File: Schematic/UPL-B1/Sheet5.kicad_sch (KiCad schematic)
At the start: 103 parts, among them P53 TestPoint, P54 TestPoint, P55 TestPoint, P56 TestPoint, P57 TestPoint, P58 TestPoint, X50 Conn_01x03_Pin_Bridge, X51 Conn_01x03_Pin_Bridge, X52 Conn_01x03_Pin_Bridge

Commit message: Add device datasheets, begin migration to hierarchical labels
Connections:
- net LDFREQ renamed LOFREQ
- no-connect marks 0 -> 2
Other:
- note added: "+/- ~15V"
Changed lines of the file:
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@@
 		)
 	)
+	(text "+/- ~15V"
+		(exclude_from_sim no)
+		(at 81.026 191.516 0)
+		(effects
+			(font
+				(size 1.27 1.27)
+			)
+		)
+	)
 	(text "SHEET 6"
 		(exclude_from_sim no)
@@
 		(color 0 0 0 0)
 	)
+	(no_connect
+		(at 353.06 171.45)
+	)
+	(no_connect
+		(at 383.54 171.45)
+	)
 	(wire
 		(pts
@@
 	(global_label "SIN"
 		(shape input)
-		(at 43.18 270.51 180)
+		(at 374.65 226.06 180)
 		(fields_autoplaced yes)
 		(effects
@@
 		)
 		(property "Intersheetrefs" "${INTERSHEET_REFS}"
-			(at 37.05 270.51 0)
+			(at 368.52 226.06 0)
 			(effects
 				(font
@@
 		)
 	)
-	(global_label "SIN"
+	(hierarchical_label "SIN"
 		(shape input)
-		(at 374.65 226.06 180)
-		(fields_autoplaced yes)
+		(at 43.18 270.51 180)
 		(effects
 			(font
@@
 			(justify right)
 		)
-		(property "Intersheetrefs" "${INTERSHEET_REFS}"
-			(at 368.52 226.06 0)
-			(effects
-				(font
-					(size 1.27 1.27)
-				)
-				(justify right)
-				(hide yes)
-			)
-		)
 	)
-	(global_label "FILT"
+	(hierarchical_label "FILT"
 		(shape input)
 		(at 43.18 191.77 180)
-		(fields_autoplaced yes)
 		(effects
 			(font
@@
 			(justify right)
 		)
-		(property "Intersheetrefs" "${INTERSHEET_REFS}"
-			(at 36.5057 191.77 0)
-			(effects
-				(font
-					(size 1.27 1.27)
-				)
-				(justify right)
-				(hide yes)
-			)
-		)
-	)
-	(global_label "FREQ_ENA"
-		(shape output)
-		(at 317.5 270.51 0)
-		(fields_autoplaced yes)
-		(effects
-			(font
-				(size 1.27 1.27)
-			)
-			(justify left)
-		)
-		(property "Intersheetrefs" "${INTERSHEET_REFS}"
-			(at 329.859 270.51 0)
-			(effects
-				(font
-					(size 1.27 1.27)
-				)
-				(justify left)
-				(hide yes)
-			)
-		)
 	)
-	(global_label "LDFREQ"
+	(hierarchical_label "LOFREQ"
 		(shape output)
 		(at 317.5 283.21 0)
-		(fields_autoplaced yes)
 		(effects
 			(font
@@
 			(justify left)
 		)
-		(property "Intersheetrefs" "${INTERSHEET_REFS}"
-			(at 327.6214 283.21 0)
-			(effects
-				(font
-					(size 1.27 1.27)
-				)
-				(justify left)
-				(hide yes)
-			)
-		)
 	)
-	(global_label "COS"
+	(hierarchical_label "COS"
 		(shape input)
 		(at 41.91 162.56 180)
-		(fields_autoplaced yes)
 		(effects
 			(font
@@
 			(justify right)
 		)
-		(property "Intersheetrefs" "${INTERSHEET_REFS}"
-			(at 35.1148 162.56 0)
-			(effects
-				(font
-					(size 1.27 1.27)
-				)
-				(justify right)
-				(hide yes)
-			)
-		)
 	)
-	(global_label "ALC"
+	(hierarchical_label "ALC"
 		(shape output)
 		(at 563.88 229.87 0)
-		(fields_autoplaced yes)
 		(effects
 			(font
@@
 			(justify left)
 		)
-		(property "Intersheetrefs" "${INTERSHEET_REFS}"
-			(at 570.2519 229.87 0)
-			(effects
-				(font
-					(size 1.27 1.27)
-				)
-				(justify left)
-				(hide yes)
-			)
-		)
 	)
-	(global_label "LOFILT"
+	(hierarchical_label "LOFILT"
 		(shape input)
 		(at 43.18 213.36 180)
-		(fields_autoplaced yes)
 		(effects
 			(font
@@
 			(justify right)
 		)
-		(property "Intersheetrefs" "${INTERSHEET_REFS}"
-			(at 34.1471 213.36 0)
-			(effects
-				(font
-					(size 1.27 1.27)
-				)
-				(justify right)
-				(hide yes)
+	)
+	(hierarchical_label "FREQ_ENA"
+		(shape output)
+		(at 317.5 270.51 0)
+		(effects
+			(font
+				(size 1.27 1.27)
 			)
+			(justify left)
 		)
 	)
@@
 			)
 		)
-		(property "Datasheet" "https://ngspice.sourceforge.io/docs/ngspice-html-manual/manual.xhtml#cha_JFETs"
+		(property "Datasheet" "https://www.mouser.de/datasheet/3/282/1/2N4091-2N4093-MIL-PRF-19500-431.PDF"
 			(at 173.99 157.48 0)
 			(effects
@@
 			)
 		)
-		(property "Datasheet" "https://ngspice.sourceforge.io/docs/ngspice-html-manual/manual.xhtml#cha_JFETs"
+		(property "Datasheet" "https://www.mouser.de/datasheet/3/282/1/2N4091-2N4093-MIL-PRF-19500-431.PDF"
 			(at 336.55 138.43 0)
 			(effects
@@
 			)
 		)
-		(property "Datasheet" "~"
+		(property "Datasheet" "https://ww1.microchip.com/downloads/aemDocuments/documents/HRDS/ProductDocuments/DataSheets/1N821-1N829A-1.pdf"
 			(at 86.36 125.73 0)
 			(effects
@@
 			)
 		)
-		(property "Datasheet" "https://ngspice.sourceforge.io/docs/ngspice-html-manual/manual.xhtml#cha_JFETs"
+		(property "Datasheet" "https://www.nxp.com/docs/en/data-sheet/BSR56_57_58.pdf"
 			(at 106.68 194.31 0)
 			(effects
@@
 			)
 		)
-		(property "Datasheet" "https://ngspice.sourceforge.io/docs/ngspice-html-manual/manual.xhtml#cha_JFETs"
+		(property "Datasheet" "https://www.mouser.de/datasheet/3/1206/1/jfet-2n4091-2n4092-2n4093-interfet.pdf"
 			(at 255.27 140.97 0)
 			(effects
@@
 			)
 		)
-		(property "Datasheet" "https://ngspice.sourceforge.io/docs/ngspice-html-manual/manual.xhtml#cha_JFETs"
+		(property "Datasheet" "https://www.nxp.com/docs/en/data-sheet/BSR56_57_58.pdf"
 			(at 106.68 215.9 0)
 			(effects
@@
 			)
 		)
-		(property "Datasheet" "~"
+		(property "Datasheet" "https://assets.nexperia.com/documents/data-sheet/BZX84_SER.pdf"
 			(at 459.74 195.58 0)
 			(effects

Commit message: update on Output IMD
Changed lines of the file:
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@@
 		)
 	)
-	(text "SHEET 6"
+	(text "SHEET 2"
 		(exclude_from_sim no)
 		(at 321.564 274.32 0)
@@
 	)
 	(hierarchical_label "FREQ_ENA"
-		(shape output)
+		(shape input)
 		(at 317.5 270.51 0)
 		(effects

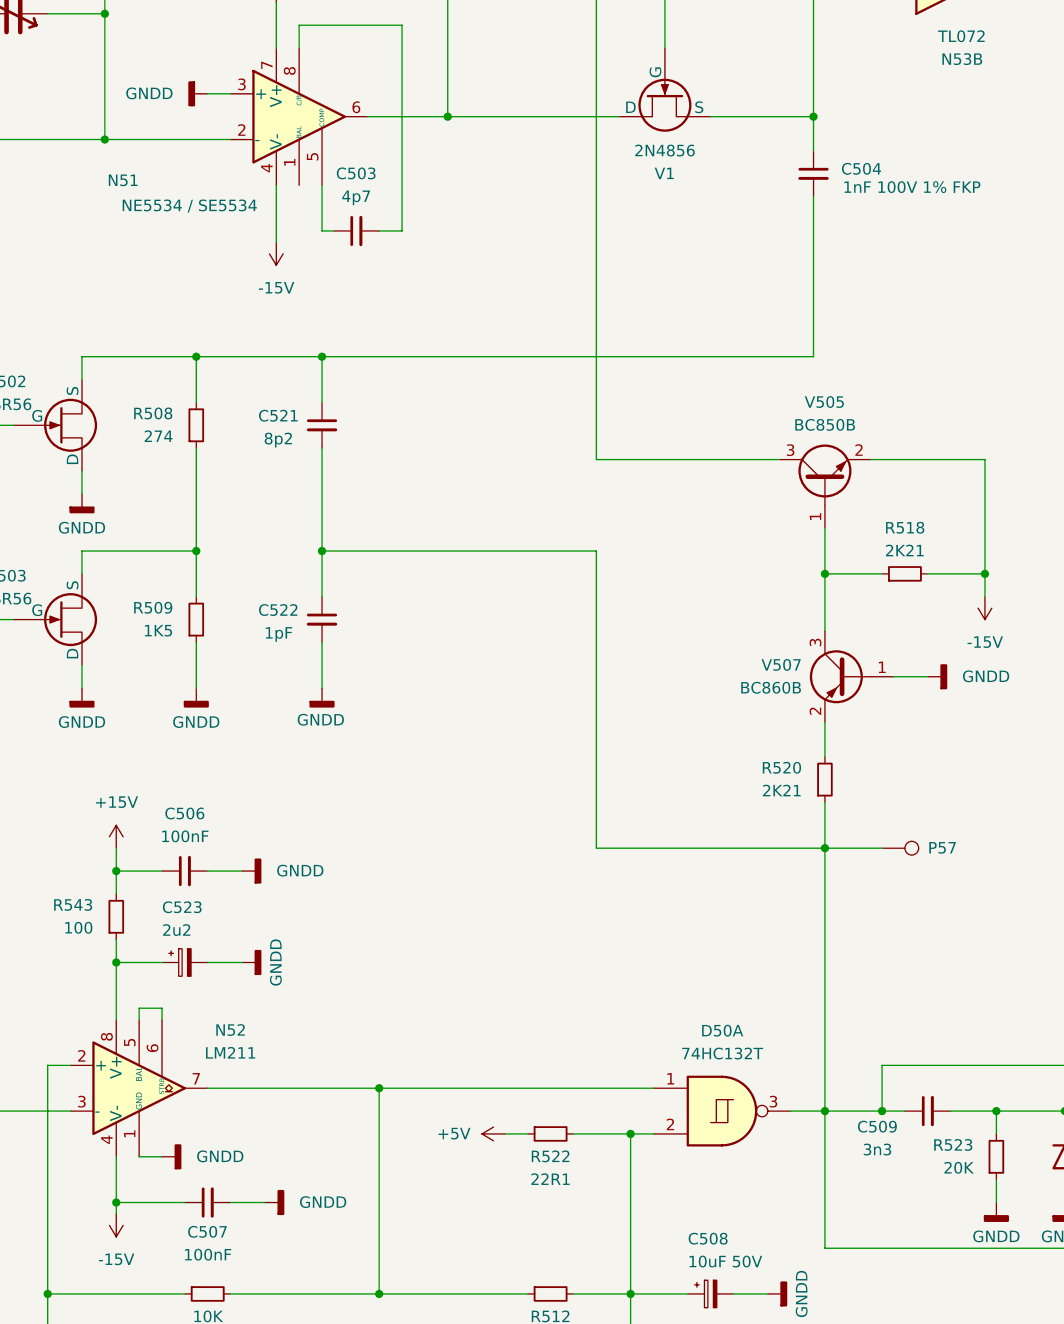
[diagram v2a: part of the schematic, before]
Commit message: Cleanup component names
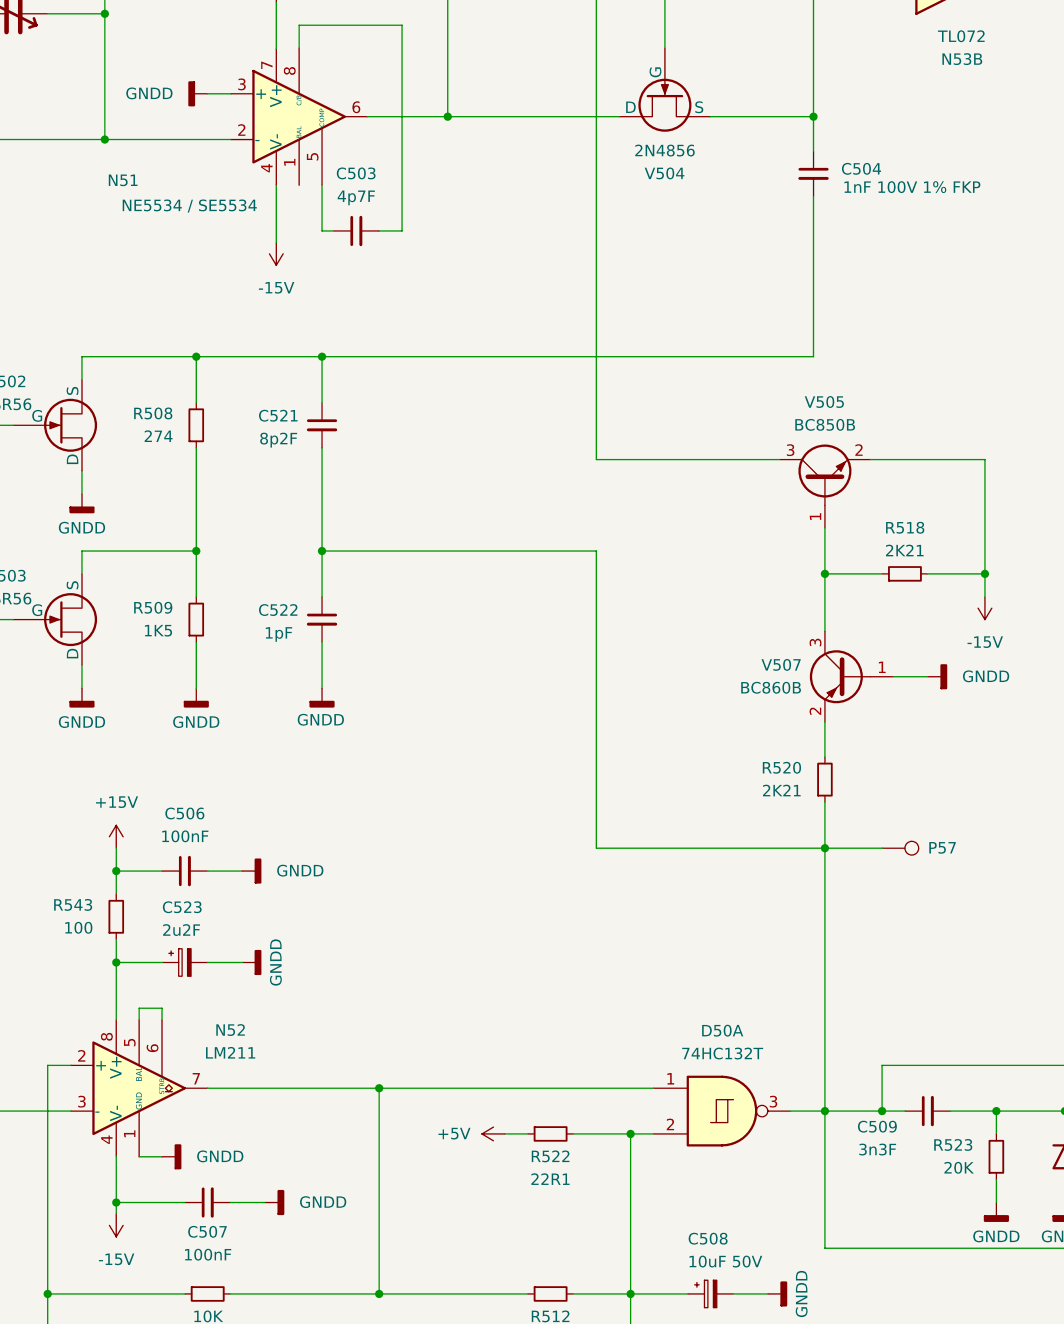
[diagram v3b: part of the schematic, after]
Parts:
- C503: value 4p7 -> 4p7F
- C509: value 3n3 -> 3n3F
- C521: value 8p2 -> 8p2F
- C523: value 2u2 -> 2u2F
- renumbered V1 to V504
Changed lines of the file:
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@@
 		(on_board yes)
 		(dnp no)
-		(property "Reference" "V1"
+		(property "Reference" "V504"
 			(at 173.99 166.37 90)
 			(effects
@@
 			(project "UPL-B1"
 				(path "/812de09b-8b67-463d-bf96-bb3aeeb1ed8d/6f377b57-c1d4-477b-840b-189645bd7d4e"
-					(reference "V1")
+					(reference "V504")
 					(unit 1)
 				)
@@
 			)
 		)
-		(property "Value" "8p2"
+		(property "Value" "8p2F"
 			(at 131.064 195.834 0)
 			(effects
@@
 			)
 		)
-		(property "Value" "3n3"
+		(property "Value" "3n3F"
 			(at 197.612 274.828 90)
 			(effects
@@
 			)
 		)
-		(property "Value" "2u2"
+		(property "Value" "2u2F"
 			(at 118.11 250.444 90)
 			(effects
@@
 			)
 		)
-		(property "Value" "4p7"
+		(property "Value" "4p7F"
 			(at 139.7063 168.91 90)
 			(effects

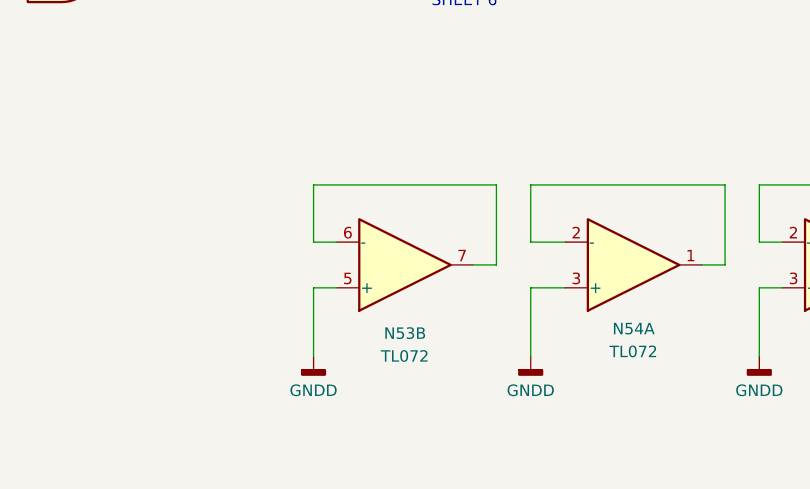
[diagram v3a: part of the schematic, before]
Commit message: Minor fixups for layout.
Reannotate, deduplicate N53B. Add some hierachical pins. First
preparations for layout
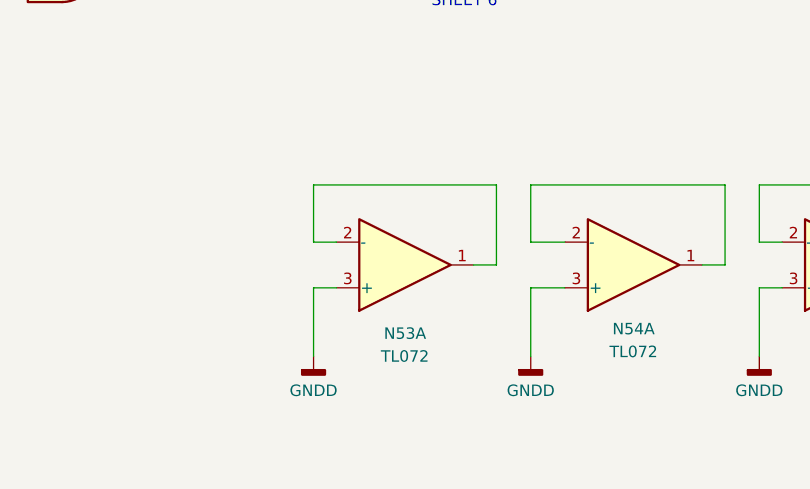
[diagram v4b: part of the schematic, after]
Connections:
- net GNDD: now also N53.3 (+); no longer N53.5 (+)
- new net: N53.1, N53.2 (-)
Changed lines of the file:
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@@
 		(at 314.96 316.23 0)
 		(mirror x)
-		(unit 2)
+		(unit 1)
 		(exclude_from_sim no)
 		(in_bom yes)
@@
 				(path "/812de09b-8b67-463d-bf96-bb3aeeb1ed8d/6f377b57-c1d4-477b-840b-189645bd7d4e"
 					(reference "N53")
-					(unit 2)
+					(unit 1)
 				)
 			)

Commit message: Group functional blocks in ALC. Begin documenting digital chain.
Fixed D21 designator, placed a few NC-Crosses on unused pins for good
practice.
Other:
- note added: "Offset"
- note added: "Offset-Referenzspannung Offset voltage reference"
- note added: "Pegelregler Level control"
- note added: "Regler Stabilizer"
- note added: "Sampler 1"
- note added: "Sampler 2"
- note added: "Schmitt-Trigger"
- note added: "T&H - Steuerung Sample & Hold control"
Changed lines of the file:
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@@
 		(company "BVKSound")
+	)
+	(rectangle
+		(start 406.4 167.64)
+		(end 579.882 275.082)
+		(stroke
+			(width 0)
+			(type dot)
+		)
+		(fill
+			(type none)
+		)
+	)
+	(rectangle
+		(start 53.848 91.186)
+		(end 102.616 138.938)
+		(stroke
+			(width 0)
+			(type dot)
+		)
+		(fill
+			(type none)
+		)
+	)
+	(rectangle
+		(start 149.352 109.728)
+		(end 235.458 172.72)
+		(stroke
+			(width 0)
+			(type dot)
+		)
+		(fill
+			(type none)
+		)
+	)
+	(rectangle
+		(start 147.32 187.96)
+		(end 288.29 299.72)
+		(stroke
+			(width 0)
+			(type dot)
+		)
+		(fill
+			(type none)
+		)
+	)
+	(rectangle
+		(start 109.474 109.728)
+		(end 148.082 181.356)
+		(stroke
+			(width 0)
+			(type dot)
+		)
+		(fill
+			(type none)
+		)
+	)
+	(rectangle
+		(start 47.752 234.188)
+		(end 145.034 308.102)
+		(stroke
+			(width 0)
+			(type dot)
+		)
+		(fill
+			(type none)
+		)
+	)
+	(rectangle
+		(start 245.11 109.728)
+		(end 326.39 172.974)
+		(stroke
+			(width 0)
+			(type dot)
+		)
+		(fill
+			(type none)
+		)
+	)
+	(rectangle
+		(start 327.66 115.062)
+		(end 399.542 161.798)
+		(stroke
+			(width 0)
+			(type dot)
+		)
+		(fill
+			(type none)
+		)
+	)
+	(text "Regler\nStabilizer"
+		(exclude_from_sim no)
+		(at 364.744 112.268 0)
+		(effects
+			(font
+				(size 1.27 1.27)
+			)
+		)
+	)
+	(text "Schmitt-Trigger"
+		(exclude_from_sim no)
+		(at 95.25 310.134 0)
+		(effects
+			(font
+				(size 1.27 1.27)
+			)
+		)
 	)
 	(text "SHEET 2"
@@
 		)
 	)
+	(text "Sampler 1"
+		(exclude_from_sim no)
+		(at 160.782 108.712 0)
+		(effects
+			(font
+				(size 1.27 1.27)
+			)
+		)
+	)
+	(text "Sampler 2"
+		(exclude_from_sim no)
+		(at 260.35 107.95 0)
+		(effects
+			(font
+				(size 1.27 1.27)
+			)
+		)
+	)
 	(text "-6V2"
 		(exclude_from_sim no)
@@
 		)
 	)
+	(text "Offset"
+		(exclude_from_sim no)
+		(at 126.746 108.458 0)
+		(effects
+			(font
+				(size 1.27 1.27)
+			)
+		)
+	)
 	(text "SHEET 3/4"
 		(exclude_from_sim no)
@@
 		(effects
 			(font
+				(size 1.27 1.27)
+			)
+		)
+	)
+	(text "Pegelregler\nLevel control"
+		(exclude_from_sim no)
+		(at 487.172 165.354 0)
+		(effects
+			(font
+				(size 1.27 1.27)
+			)
+		)
+	)
+	(text "Offset-Referenzspannung\nOffset voltage reference"
+		(exclude_from_sim no)
+		(at 76.962 89.154 0)
+		(effects
+			(font
+				(size 1.27 1.27)
+			)
+		)
+	)
+	(text "T&H - Steuerung\nSample & Hold control"
+		(exclude_from_sim no)
+		(at 273.304 302.26 0)
+		(effects
+			(font
